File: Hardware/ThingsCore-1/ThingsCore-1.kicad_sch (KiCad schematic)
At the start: 0 parts

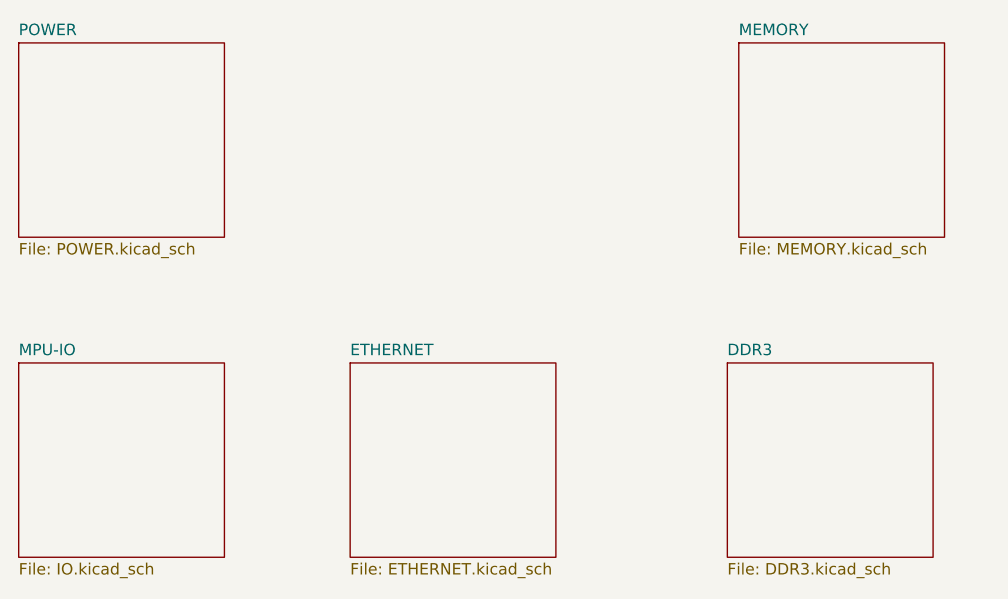
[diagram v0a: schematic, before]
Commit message: ddr3 fanout done
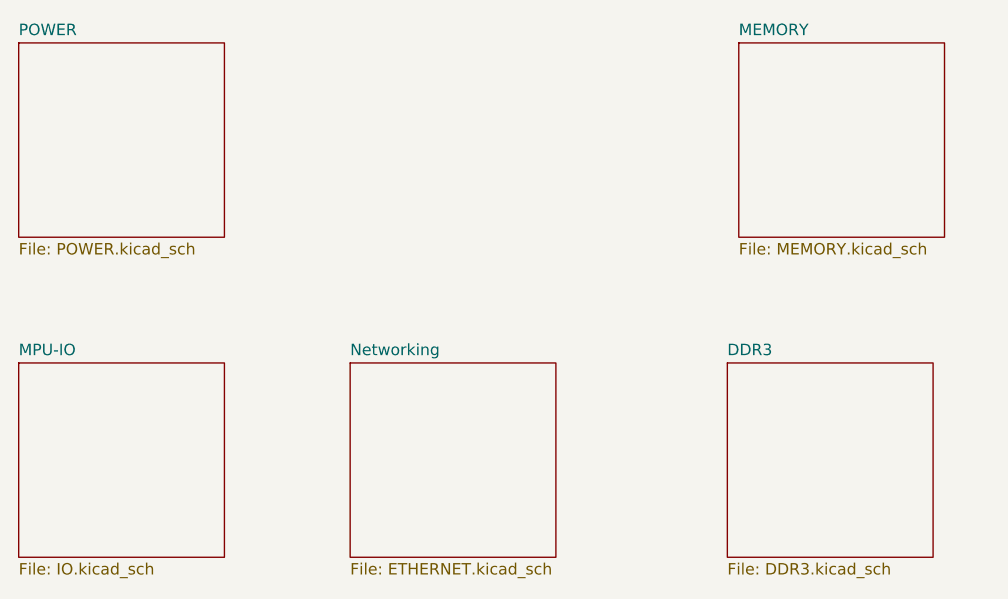
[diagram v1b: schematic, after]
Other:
- sheet ETHERNET renamed Networking
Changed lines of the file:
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@@
 			(color 0 0 0 0.0000)
 		)
-		(property "Sheetname" "ETHERNET"
+		(property "Sheetname" "Networking"
 			(at 106.68 109.7784 0)
 			(effects

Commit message: layout transciever components, pin selection and last components
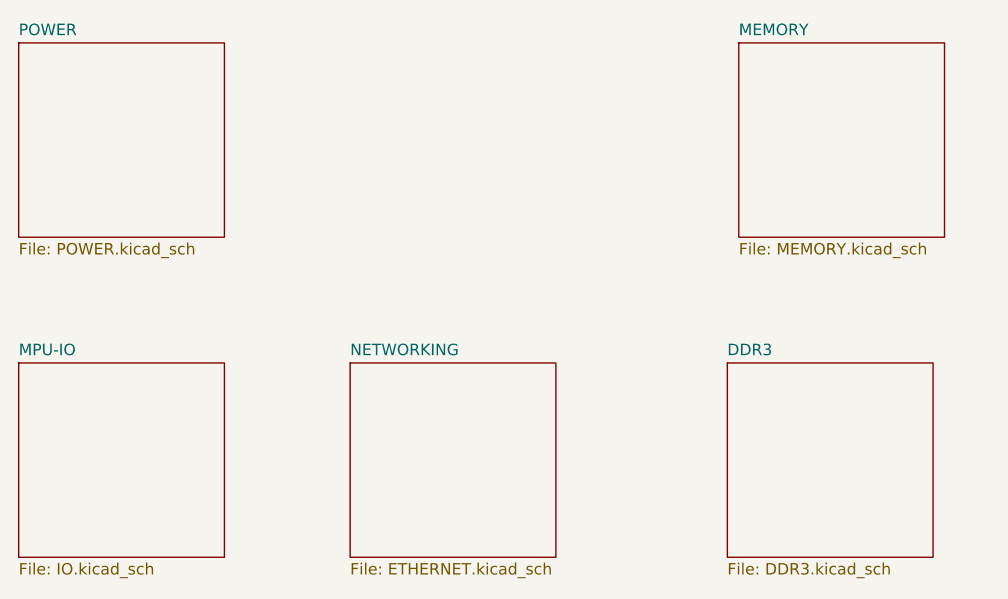
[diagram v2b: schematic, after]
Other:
- sheet Networking renamed NETWORKING
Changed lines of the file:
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@@
 			(color 0 0 0 0.0000)
 		)
-		(property "Sheetname" "Networking"
+		(property "Sheetname" "NETWORKING"
 			(at 106.68 109.7784 0)
 			(effects
